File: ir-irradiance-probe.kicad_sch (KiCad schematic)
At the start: 40 parts, among them J2 SM04B-SRSS-TB-LF-SN, J3 PinHeader_1x2_P2.54mm_Drill1.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

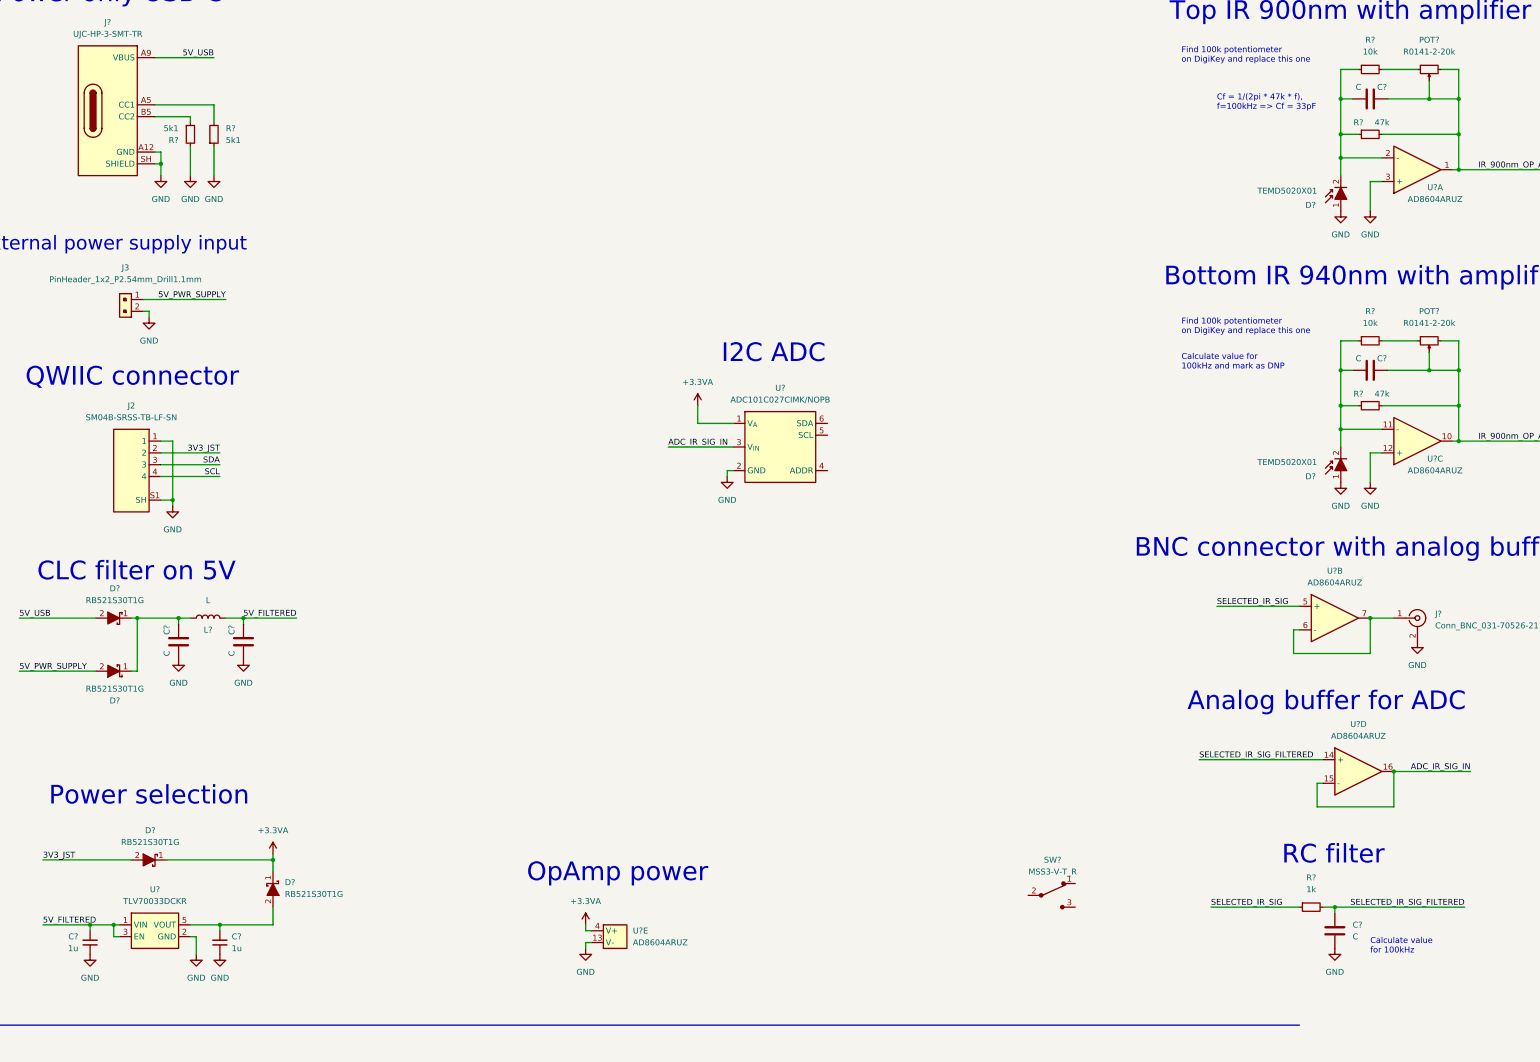
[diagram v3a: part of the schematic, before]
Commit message: [#47284] Update RC filter with C value
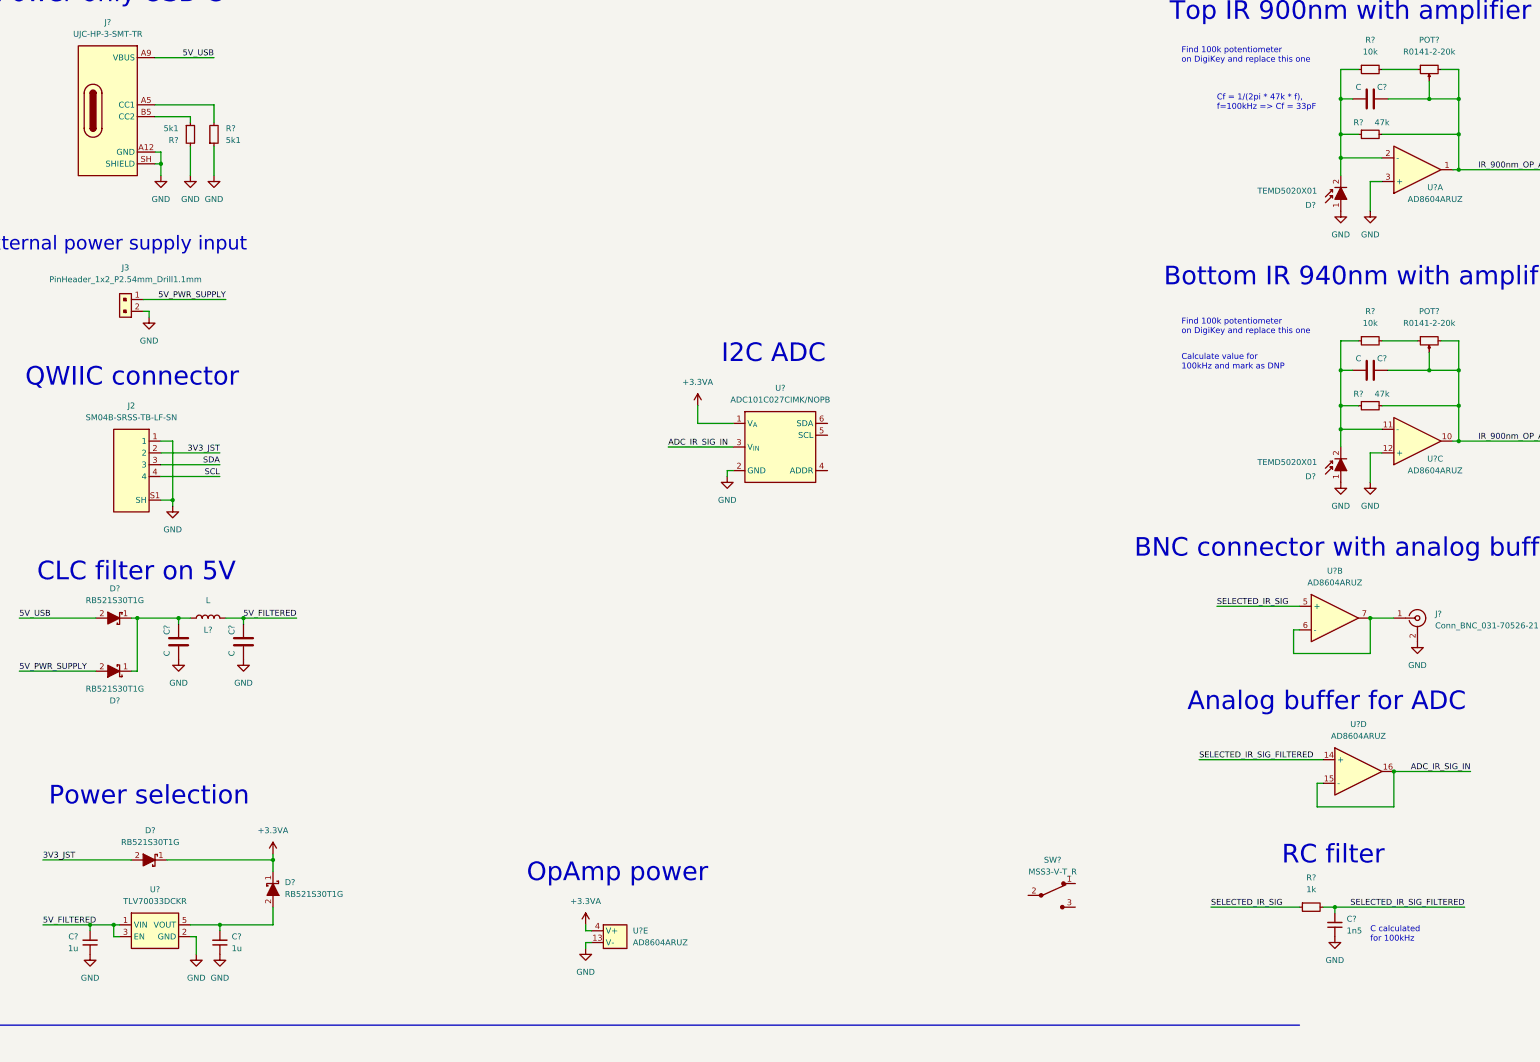
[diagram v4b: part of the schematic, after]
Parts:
- removed C?: C, symbol Device:C
- added C?: C_1n5_0402, antmicro-footprints:C_0402_1005Metric, symbol Capacitors0402:C_1n5_0402
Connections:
- net GND: now also C?.1
- net SELECTED_IR_SIG_FILTERED: now also C?.2
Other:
- note added: "C calculated for 100kHz"
- note removed: "Calculate value for 100kHz"

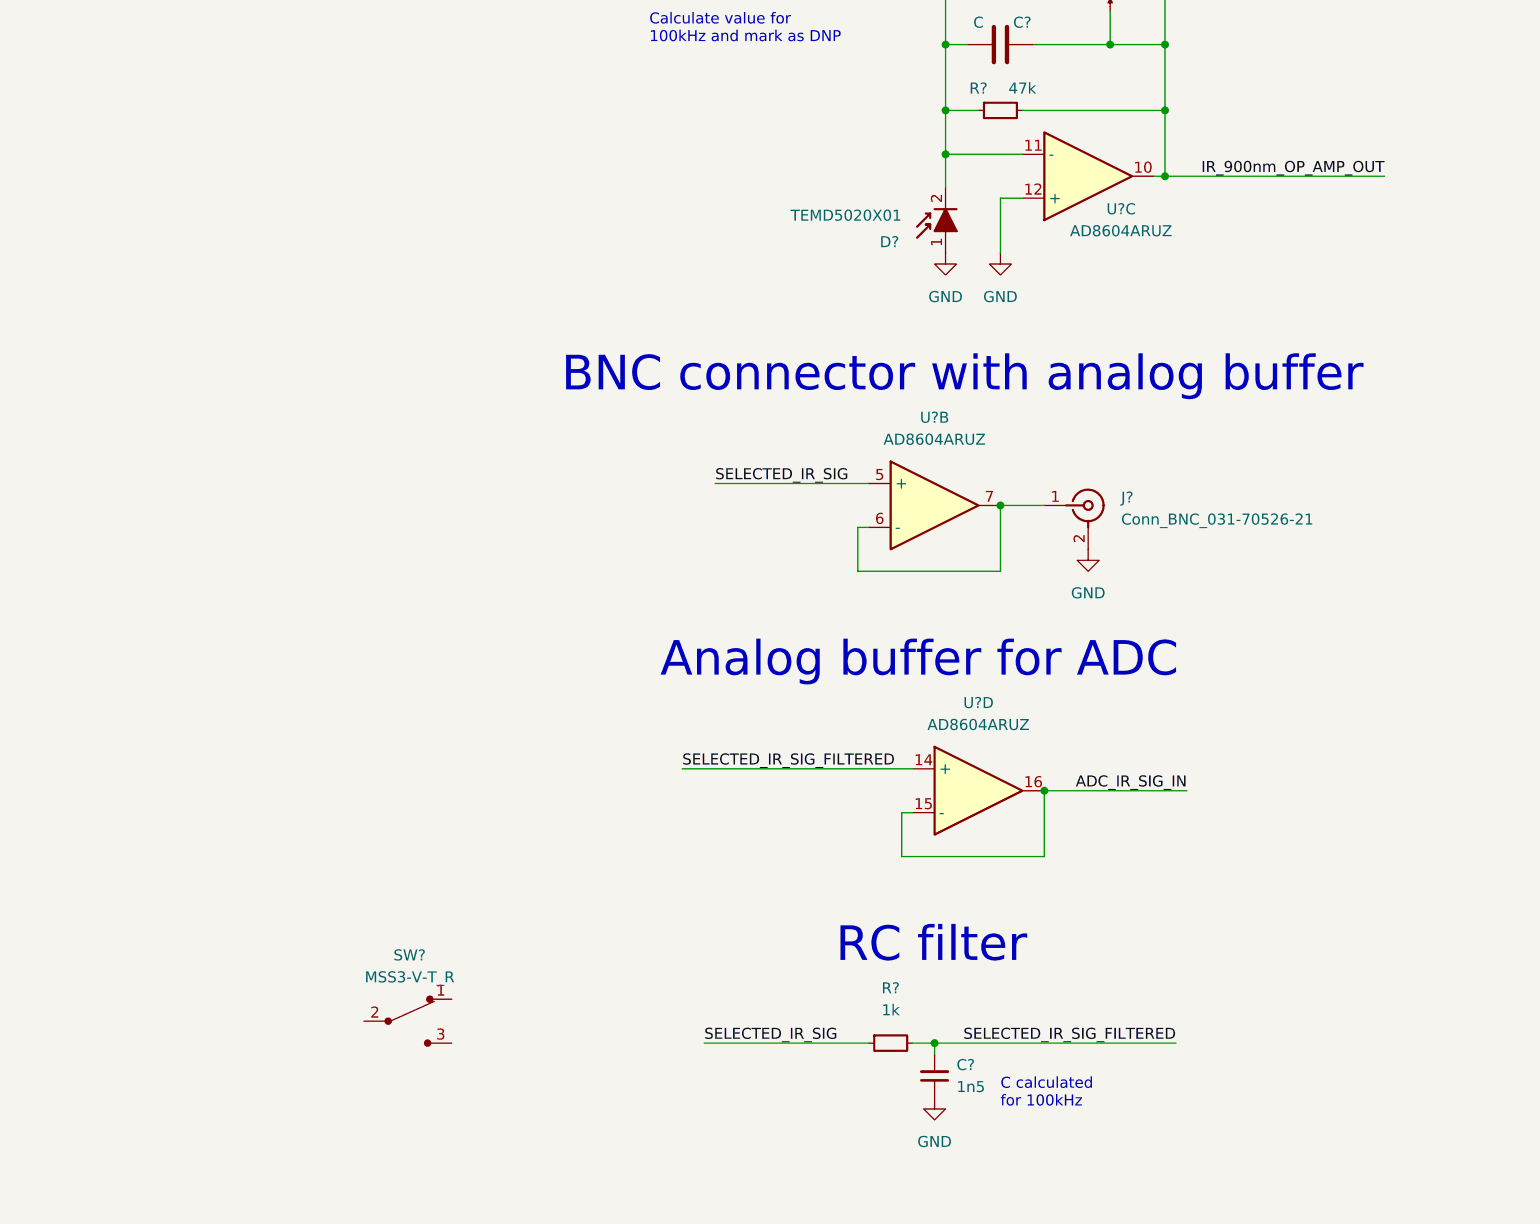
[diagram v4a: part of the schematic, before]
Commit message: [#47284] Connect IR signals to the switch
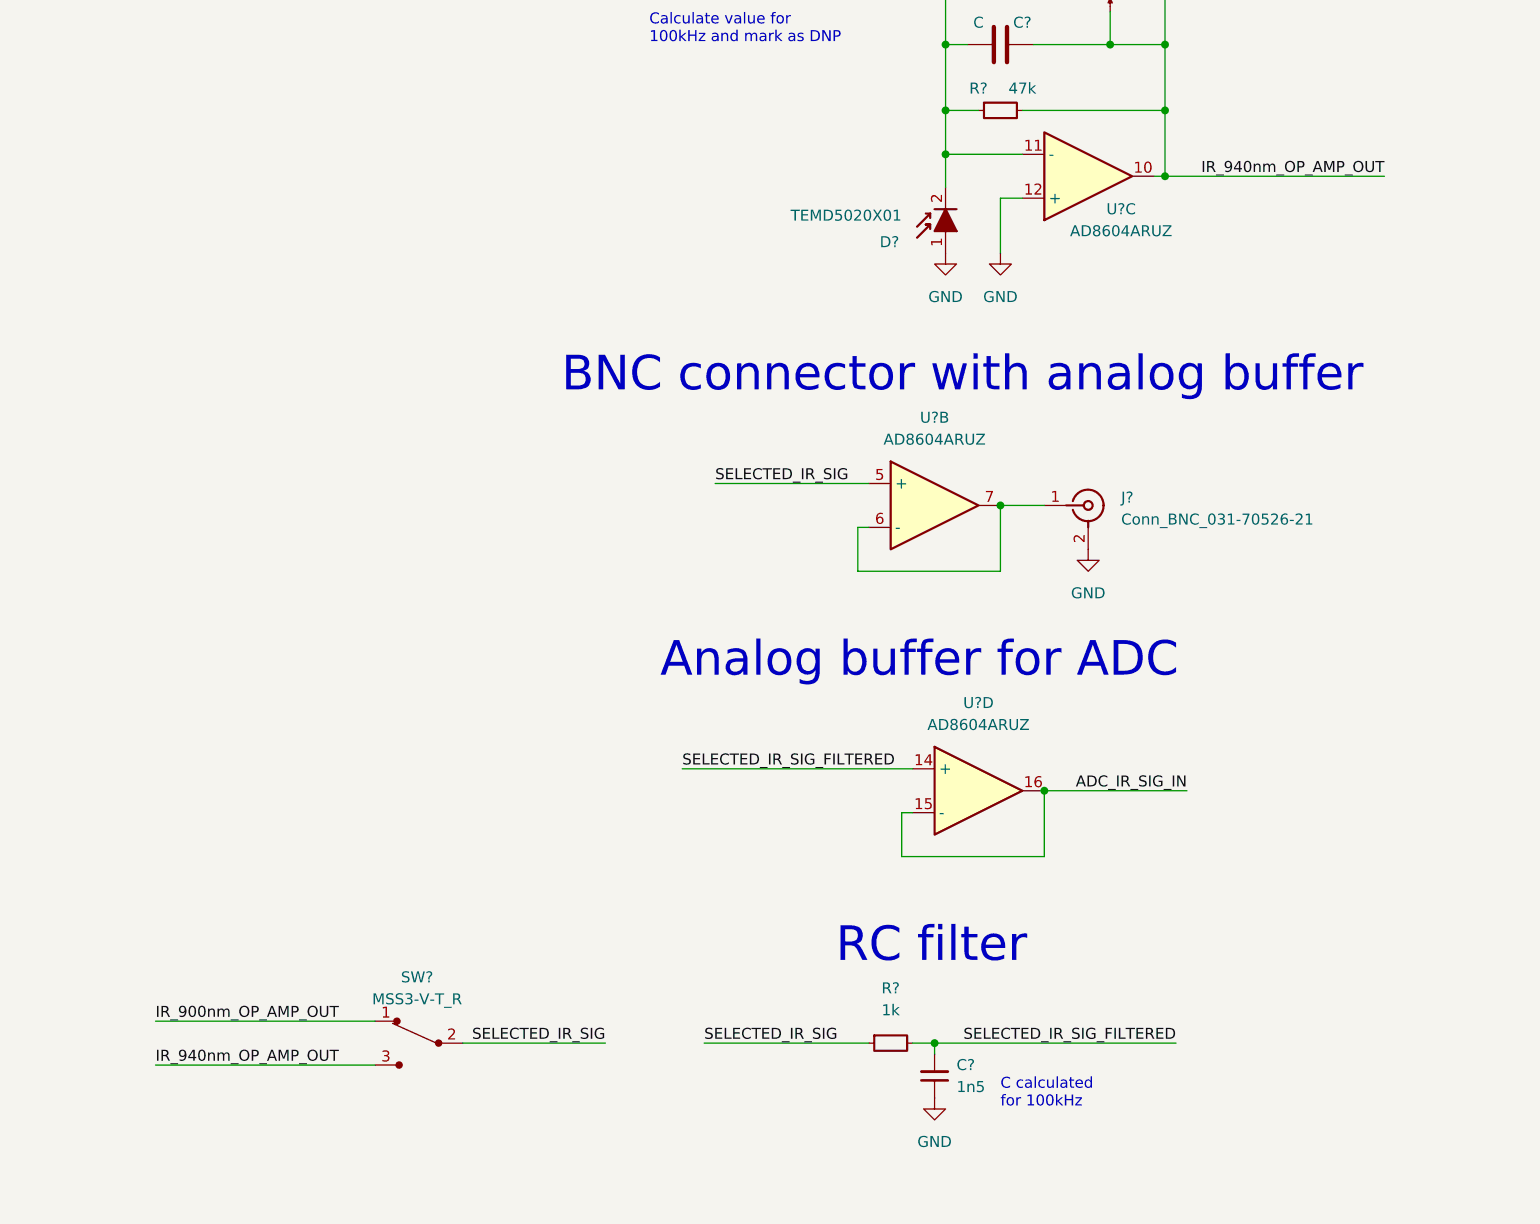
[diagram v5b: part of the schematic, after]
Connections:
- net IR_900nm_OP_AMP_OUT: now also SW?.1; no longer C?.2, POT?.2, POT?.3, R?.2, U?.10
- net SELECTED_IR_SIG: now also SW?.2
- net IR_940nm_OP_AMP_OUT: now reaches SW?.3
- net IR_940nm_OP_AMP_OUT: now also C?.2, POT?.2, POT?.3, R?.2, U?.10
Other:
- moved on the sheet: SW?
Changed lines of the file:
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@@
+    (stroke (width 0) (type default))
+  )
+  (wire (pts (xy 217.17 224.79) (xy 242.57 224.79))
     (stroke (width 0) (type default))
   )
@@
     (stroke (width 0) (type default))
   )
+  (wire (pts (xy 252.73 227.33) (xy 269.24 227.33))
+    (stroke (width 0) (type default))
+  )
   (wire (pts (xy 308.61 111.76) (xy 308.61 119.38))
     (stroke (width 0) (type default))
@@
   )
   (wire (pts (xy 54.61 139.7) (xy 57.15 139.7))
+    (stroke (width 0) (type default))
+  )
+  (wire (pts (xy 217.17 229.87) (xy 242.57 229.87))
     (stroke (width 0) (type default))
   )
@@
     (effects (font (size 1.27 1.27)) (justify right bottom))
   )
+  (label "SELECTED_IR_SIG" (at 269.24 227.33 180) (fields_autoplaced)
+    (effects (font (size 1.27 1.27)) (justify right bottom))
+  )
   (label "5V_PWR_SUPPLY" (at 24.13 176.53 0) (fields_autoplaced)
     (effects (font (size 1.27 1.27)) (justify left bottom))
@@
     (effects (font (size 1.27 1.27)) (justify left bottom))
   )
+  (label "IR_940nm_OP_AMP_OUT" (at 217.17 229.87 0) (fields_autoplaced)
+    (effects (font (size 1.27 1.27)) (justify left bottom))
+  )
   (label "SELECTED_IR_SIG_FILTERED" (at 335.28 227.33 180) (fields_autoplaced)
     (effects (font (size 1.27 1.27)) (justify right bottom))
   )
+  (label "IR_900nm_OP_AMP_OUT" (at 217.17 224.79 0) (fields_autoplaced)
+    (effects (font (size 1.27 1.27)) (justify left bottom))
+  )
   (label "5V_PWR_SUPPLY" (at 68.58 96.52 180) (fields_autoplaced)
     (effects (font (size 1.27 1.27)) (justify right bottom))
@@
     (effects (font (size 1.27 1.27)) (justify right bottom))
   )
-  (label "IR_900nm_OP_AMP_OUT" (at 359.41 127 180) (fields_autoplaced)
+  (label "IR_940nm_OP_AMP_OUT" (at 359.41 127 180) (fields_autoplaced)
     (effects (font (size 1.27 1.27)) (justify right bottom))
   )
@@
     )
   )
-  (symbol (lib_id "antmicroSlideSwitches:MSS3-V-T_R") (at 246.38 224.79 0) (unit 1)
-    (in_bom yes) (on_board yes) (dnp no) (fields_autoplaced)
-    (property "Reference" "SW?" (at 246.5832 217.17 0)
+  (symbol (lib_id "antmicroSlideSwitches:MSS3-V-T_R") (at 247.65 227.33 0) (mirror y) (unit 1)
+    (in_bom yes) (on_board yes) (dnp no)
+    (property "Reference" "SW?" (at 247.4468 219.71 0)
       (effects (font (size 1.27 1.27)))
     )
-    (property "Value" "MSS3-V-T_R" (at 246.5832 219.71 0)
+    (property "Value" "MSS3-V-T_R" (at 247.4468 222.25 0)
       (effects (font (size 1.27 1.27)))
     )
-    (property "Footprint" "antmicro-footprints:Switch_Slide_MSS3" (at 251.46 219.71 0)
+    (property "Footprint" "antmicro-footprints:Switch_Slide_MSS3" (at 242.57 222.25 0)
       (effects (font (size 1.27 1.27)) (justify left) hide)
     )
-    (property "Datasheet" "https://pl.mouser.com/datasheet/2/910/605_MSS34-1571494.pdf" (at 251.46 217.17 0)
+    (property "Datasheet" "https://pl.mouser.com/datasheet/2/910/605_MSS34-1571494.pdf" (at 242.57 219.71 0)
       (effects (font (size 1.524 1.524)) (justify left) hide)
     )
-    (property "MPN" "MSS3-V-T/R" (at 251.46 212.09 0)
+    (property "MPN" "MSS3-V-T/R" (at 242.57 214.63 0)
       (effects (font (size 1.524 1.524)) (justify left) hide)
     )
-    (property "Manufacturer" "Diptronics" (at 251.46 209.042 0)
+    (property "Manufacturer" "Diptronics" (at 242.57 211.582 0)
       (effects (font (size 1.524 1.524)) (justify left) hide)
     )
